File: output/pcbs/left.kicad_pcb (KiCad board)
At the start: 2 copper layers, 151.8 x 117.2 mm, 85 parts

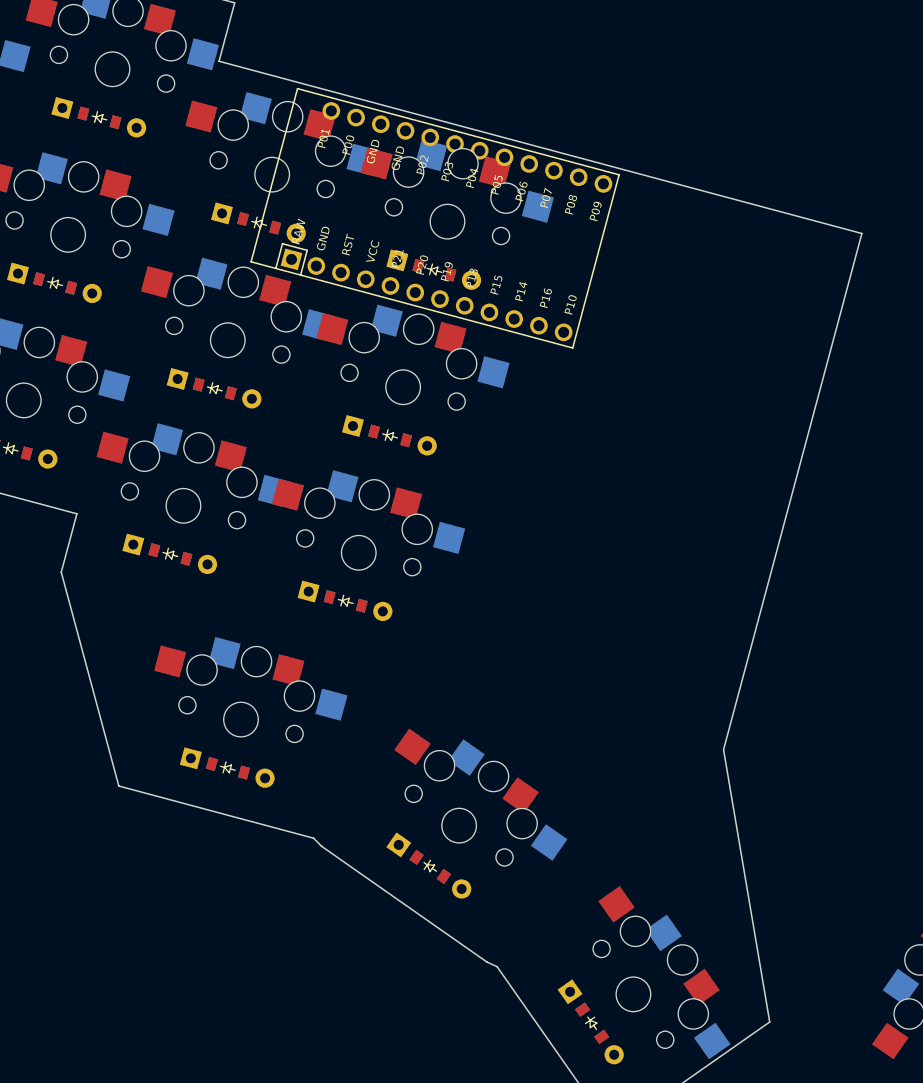
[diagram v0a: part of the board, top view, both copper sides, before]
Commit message: run ergogen with new case
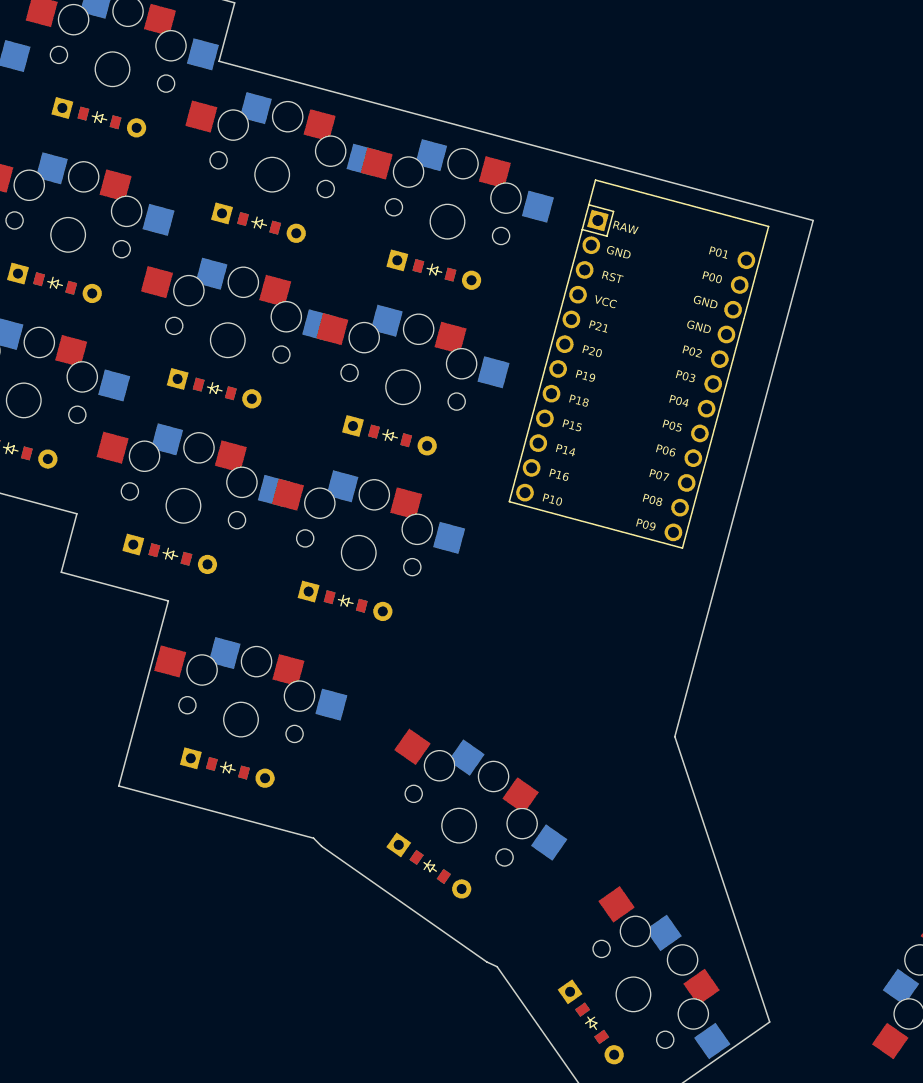
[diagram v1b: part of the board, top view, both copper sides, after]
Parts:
- moved MCU1 24.2 mm to (117.2, -4.82), turned to -105 degrees
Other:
- board size 151.8 x 117.2 mm -> 147 x 117.2 mm
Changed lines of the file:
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@@
     )
       (module ProMicro (layer F.Cu)
-      (at 98.5801815 -20.1729481 -15)
+      (at 117.2423592 -4.819670799999999 -105)
       (fp_text reference "MCU1" (at 0 0) (layer F.SilkS) hide (effects (font (size 1.27 1.27) (thickness 0.15))))
       (fp_text value "" (at 0 0) (layer F.SilkS) hide (effects (font (size 1.27 1.27) (thickness 0.15))))
@@
         (fp_line (start -15.24 6.35) (end -15.24 8.89) (layer F.SilkS) (width 0.15))
         (fp_line (start -12.7 6.35) (end -12.7 8.89) (layer F.SilkS) (width 0.15))
-        (fp_text user RAW (at -13.97 4.8 75) (layer F.SilkS) (effects (font (size 0.8 0.8) (thickness 0.15))))
-        (fp_text user GND (at -11.43 4.8 75) (layer F.SilkS) (effects (font (size 0.8 0.8) (thickness 0.15))))
-        (fp_text user RST (at -8.89 4.8 75) (layer F.SilkS) (effects (font (size 0.8 0.8) (thickness 0.15))))
-        (fp_text user VCC (at -6.35 4.8 75) (layer F.SilkS) (effects (font (size 0.8 0.8) (thickness 0.15))))
-        (fp_text user P21 (at -3.81 4.8 75) (layer F.SilkS) (effects (font (size 0.8 0.8) (thickness 0.15))))
-        (fp_text user P20 (at -1.27 4.8 75) (layer F.SilkS) (effects (font (size 0.8 0.8) (thickness 0.15))))
-        (fp_text user P19 (at 1.27 4.8 75) (layer F.SilkS) (effects (font (size 0.8 0.8) (thickness 0.15))))
-        (fp_text user P18 (at 3.81 4.8 75) (layer F.SilkS) (effects (font (size 0.8 0.8) (thickness 0.15))))
-        (fp_text user P15 (at 6.35 4.8 75) (layer F.SilkS) (effects (font (size 0.8 0.8) (thickness 0.15))))
-        (fp_text user P14 (at 8.89 4.8 75) (layer F.SilkS) (effects (font (size 0.8 0.8) (thickness 0.15))))
-        (fp_text user P16 (at 11.43 4.8 75) (layer F.SilkS) (effects (font (size 0.8 0.8) (thickness 0.15))))
-        (fp_text user P10 (at 13.97 4.8 75) (layer F.SilkS) (effects (font (size 0.8 0.8) (thickness 0.15))))
-        (fp_text user P01 (at -13.97 -4.8 75) (layer F.SilkS) (effects (font (size 0.8 0.8) (thickness 0.15))))
-        (fp_text user P00 (at -11.43 -4.8 75) (layer F.SilkS) (effects (font (size 0.8 0.8) (thickness 0.15))))
-        (fp_text user GND (at -8.89 -4.8 75) (layer F.SilkS) (effects (font (size 0.8 0.8) (thickness 0.15))))
-        (fp_text user GND (at -6.35 -4.8 75) (layer F.SilkS) (effects (font (size 0.8 0.8) (thickness 0.15))))
-        (fp_text user P02 (at -3.81 -4.8 75) (layer F.SilkS) (effects (font (size 0.8 0.8) (thickness 0.15))))
-        (fp_text user P03 (at -1.27 -4.8 75) (layer F.SilkS) (effects (font (size 0.8 0.8) (thickness 0.15))))
-        (fp_text user P04 (at 1.27 -4.8 75) (layer F.SilkS) (effects (font (size 0.8 0.8) (thickness 0.15))))
-        (fp_text user P05 (at 3.81 -4.8 75) (layer F.SilkS) (effects (font (size 0.8 0.8) (thickness 0.15))))
-        (fp_text user P06 (at 6.35 -4.8 75) (layer F.SilkS) (effects (font (size 0.8 0.8) (thickness 0.15))))
-        (fp_text user P07 (at 8.89 -4.8 75) (layer F.SilkS) (effects (font (size 0.8 0.8) (thickness 0.15))))
-        (fp_text user P08 (at 11.43 -4.8 75) (layer F.SilkS) (effects (font (size 0.8 0.8) (thickness 0.15))))
-        (fp_text user P09 (at 13.97 -4.8 75) (layer F.SilkS) (effects (font (size 0.8 0.8) (thickness 0.15))))
-        (pad 1 thru_hole rect (at -13.97 7.62 -15) (size 1.7526 1.7526) (drill 1.0922) (layers *.Cu *.SilkS *.Mask) (net 43 "RAW"))
+        (fp_text user RAW (at -13.97 4.8 -15) (layer F.SilkS) (effects (font (size 0.8 0.8) (thickness 0.15))))
+        (fp_text user GND (at -11.43 4.8 -15) (layer F.SilkS) (effects (font (size 0.8 0.8) (thickness 0.15))))
+        (fp_text user RST (at -8.89 4.8 -15) (layer F.SilkS) (effects (font (size 0.8 0.8) (thickness 0.15))))
+        (fp_text user VCC (at -6.35 4.8 -15) (layer F.SilkS) (effects (font (size 0.8 0.8) (thickness 0.15))))
+        (fp_text user P21 (at -3.81 4.8 -15) (layer F.SilkS) (effects (font (size 0.8 0.8) (thickness 0.15))))
+        (fp_text user P20 (at -1.27 4.8 -15) (layer F.SilkS) (effects (font (size 0.8 0.8) (thickness 0.15))))
+        (fp_text user P19 (at 1.27 4.8 -15) (layer F.SilkS) (effects (font (size 0.8 0.8) (thickness 0.15))))
+        (fp_text user P18 (at 3.81 4.8 -15) (layer F.SilkS) (effects (font (size 0.8 0.8) (thickness 0.15))))
+        (fp_text user P15 (at 6.35 4.8 -15) (layer F.SilkS) (effects (font (size 0.8 0.8) (thickness 0.15))))
+        (fp_text user P14 (at 8.89 4.8 -15) (layer F.SilkS) (effects (font (size 0.8 0.8) (thickness 0.15))))
+        (fp_text user P16 (at 11.43 4.8 -15) (layer F.SilkS) (effects (font (size 0.8 0.8) (thickness 0.15))))
+        (fp_text user P10 (at 13.97 4.8 -15) (layer F.SilkS) (effects (font (size 0.8 0.8) (thickness 0.15))))
+        (fp_text user P01 (at -13.97 -4.8 -15) (layer F.SilkS) (effects (font (size 0.8 0.8) (thickness 0.15))))
+        (fp_text user P00 (at -11.43 -4.8 -15) (layer F.SilkS) (effects (font (size 0.8 0.8) (thickness 0.15))))
+        (fp_text user GND (at -8.89 -4.8 -15) (layer F.SilkS) (effects (font (size 0.8 0.8) (thickness 0.15))))
+        (fp_text user GND (at -6.35 -4.8 -15) (layer F.SilkS) (effects (font (size 0.8 0.8) (thickness 0.15))))
+        (fp_text user P02 (at -3.81 -4.8 -15) (layer F.SilkS) (effects (font (size 0.8 0.8) (thickness 0.15))))
+        (fp_text user P03 (at -1.27 -4.8 -15) (layer F.SilkS) (effects (font (size 0.8 0.8) (thickness 0.15))))
+        (fp_text user P04 (at 1.27 -4.8 -15) (layer F.SilkS) (effects (font (size 0.8 0.8) (thickness 0.15))))
+        (fp_text user P05 (at 3.81 -4.8 -15) (layer F.SilkS) (effects (font (size 0.8 0.8) (thickness 0.15))))
+        (fp_text user P06 (at 6.35 -4.8 -15) (layer F.SilkS) (effects (font (size 0.8 0.8) (thickness 0.15))))
+        (fp_text user P07 (at 8.89 -4.8 -15) (layer F.SilkS) (effects (font (size 0.8 0.8) (thickness 0.15))))
+        (fp_text user P08 (at 11.43 -4.8 -15) (layer F.SilkS) (effects (font (size 0.8 0.8) (thickness 0.15))))
+        (fp_text user P09 (at 13.97 -4.8 -15) (layer F.SilkS) (effects (font (size 0.8 0.8) (thickness 0.15))))
+        (pad 1 thru_hole rect (at -13.97 7.62 -105) (size 1.7526 1.7526) (drill 1.0922) (layers *.Cu *.SilkS *.Mask) (net 43 "RAW"))
         (pad 2 thru_hole circle (at -11.43 7.62 0) (size 1.7526 1.7526) (drill 1.0922) (layers *.Cu *.SilkS *.Mask) (net 44 "GND"))
         (pad 3 thru_hole circle (at -8.89 7.62 0) (size 1.7526 1.7526) (drill 1.0922) (layers *.Cu *.SilkS *.Mask) (net 45 "RST"))
@@
 (gr_line (start 46.3737309 4.6612324) (end 61.8285441 8.802337099999999) (angle 90) (layer Edge.Cuts) (width 0.15))
 (gr_line (start 61.8285441 8.802337099999999) (end 60.275629800000004 14.597892000000002) (angle 90) (layer Edge.Cuts) (width 0.15))
-(gr_line (start 60.275629800000004 14.597892000000002) (end 65.98325200000001 35.7974923) (angle 90) (layer Edge.Cuts) (width 0.15))
+(gr_line (start 60.275629800000004 14.597892000000002) (end 70.9008139 17.4449015) (angle 90) (layer Edge.Cuts) (width 0.15))
+(gr_line (start 70.9008139 17.4449015) (end 65.98325200000001 35.7974923) (angle 90) (layer Edge.Cuts) (width 0.15))
 (gr_line (start 65.98325200000001 35.7974923) (end 85.30176850000001 40.9738732) (angle 90) (layer Edge.Cuts) (width 0.15))
 (gr_line (start 85.30176850000001 40.9738732) (end 86.09494289999999 41.7748356) (angle 90) (layer Edge.Cuts) (width 0.15))
@@
 (gr_line (start 103.50192390000001 53.717759300000004) (end 114.9734526 70.10080020000001) (angle 90) (layer Edge.Cuts) (width 0.15))
 (gr_line (start 114.9734526 70.10080020000001) (end 130.5373415 59.2028479) (angle 90) (layer Edge.Cuts) (width 0.15))
-(gr_line (start 130.5373415 59.2028479) (end 125.958586 32.1975872) (angle 90) (layer Edge.Cuts) (width 0.15))
-(gr_line (start 125.958586 32.1975872) (end 139.6759955 -18.9964816) (angle 90) (layer Edge.Cuts) (width 0.15))
-(gr_line (start 139.6759955 -18.9964816) (end 75.9248909 -36.078538699999996) (angle 90) (layer Edge.Cuts) (width 0.15))
+(gr_line (start 130.5373415 59.2028479) (end 121.1289569 30.9034919) (angle 90) (layer Edge.Cuts) (width 0.15))
+(gr_line (start 121.1289569 30.9034919) (end 134.8463663 -20.290576899999998) (angle 90) (layer Edge.Cuts) (width 0.15))
+(gr_line (start 134.8463663 -20.290576899999998) (end 75.9248909 -36.078538699999996) (angle 90) (layer Edge.Cuts) (width 0.15))
 (gr_line (start 75.9248909 -36.078538699999996) (end 77.47780519999999 -41.874093699999996) (angle 90) (layer Edge.Cuts) (width 0.15))
 (gr_line (start 77.47780519999999 -41.874093699999996) (end 58.15928869999999 -47.0504746) (angle 90) (layer Edge.Cuts) (width 0.15))

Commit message: add nrf footprint
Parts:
- MCU1: value (none) -> xiao-ble; footprint ProMicro -> XIAO-BLE
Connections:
- MCU1 pad 1: RAW -> P0
- MCU1 pad 10: P14 -> P9
- MCU1 pad 11: P16 -> P10
- MCU1 pad 12: P10 -> RAW3V3
- MCU1 pad 13: P1 -> GND
- MCU1 pad 14: P0 -> RAW5V
- MCU1 pad 15: GND -> SWCLK
- MCU1 pad 16: GND -> SWDIO
- MCU1 pad 17: P2 -> GND
- MCU1 pad 18: P3 -> RST
- MCU1 pad 19: P4 -> BAT_POS
- MCU1 pad 2: GND -> P1
- MCU1 pad 20: P5 -> BAT_NEG
- MCU1 pad 21: P6 -> NFC0
- MCU1 pad 22: P7 -> NFC1
- MCU1 pad 3: RST -> P2
- MCU1 pad 4: VCC -> P3
- MCU1 pad 5: P21 -> P4
- MCU1 pad 6: P20 -> P5
- MCU1 pad 7: P19 -> P6
- MCU1 pad 8: P18 -> P7
- MCU1 pad 9: P15 -> P8

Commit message: use kicad to export example switchplate
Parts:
- moved MCU1 8.00 mm to (119.3, -12.5), turned to -15 degrees
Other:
- net class Default removed

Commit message: redo the outlines lololol
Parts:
- added D43: , ComboDiode, F.Cu at (256.8, 63.5)
- added D44: , ComboDiode, F.Cu at (247.1, 49.5)
- added S43: , PG1350, F.Cu at (254.0, 59.4)
- added S44: , PG1350, F.Cu at (244.2, 45.4)
- moved D22 177.8 mm to (96.5, 49.5), turned to -35 degrees
- moved S22 174.0 mm to (99.4, 45.4), turned to -35 degrees
- moved S42 110.7 mm to (259.0, 35.1), turned to 35 degrees
- moved D42 109.3 mm to (261.8, 39.2), turned to 35 degrees
- moved D41 101.6 mm to (271.6, 53.1)
- moved S41 101.6 mm to (268.7, 49.0)
- moved D34 93.9 mm to (279.5, -30.5)
- moved S34 93.9 mm to (278.2, -35.3)
- moved S25 92.8 mm to (334.8, -32.8)
- moved S37 92.8 mm to (262.4, -24.8)
- moved D25 92.8 mm to (336.1, -28.0)
- moved D37 92.8 mm to (263.7, -20.0)
- moved D31 92.1 mm to (298.2, -30.3)
- moved S31 92.1 mm to (296.9, -35.1)
- moved D28 91.7 mm to (318.7, -23.4)
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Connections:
- net far_thumb renamed right_bottom
- net home_thumb renamed left_top
- net mirror_far_thumb renamed mirror_left_top
- net mirror_home_thumb renamed mirror_left_bottom
- net near_thumb renamed left_bottom
- D22 pad 2: mirror_outer_bottom -> right_top
- D23 pad 2: mirror_outer_home -> mirror_outer_bottom
- D24 pad 2: mirror_outer_top -> mirror_outer_home
- D25 pad 2: mirror_pinky_bottom -> mirror_outer_top
- D26 pad 2: mirror_pinky_home -> mirror_pinky_bottom
- D27 pad 2: mirror_pinky_top -> mirror_pinky_home
- D28 pad 2: mirror_ring_bottom -> mirror_pinky_top
- D29 pad 2: mirror_ring_home -> mirror_ring_bottom
- D30 pad 2: mirror_ring_top -> mirror_ring_home
- D31 pad 2: mirror_middle_bottom -> mirror_ring_top
- D32 pad 2: mirror_middle_home -> mirror_middle_bottom
- D33 pad 2: mirror_middle_top -> mirror_middle_home
- D34 pad 2: mirror_index_bottom -> mirror_middle_top
- D35 pad 2: mirror_index_home -> mirror_index_bottom
- D36 pad 2: mirror_index_top -> mirror_index_home
- D37 pad 2: mirror_inner_bottom -> mirror_index_top
- D38 pad 2: mirror_inner_home -> mirror_inner_bottom
- D39 pad 2: mirror_inner_top -> mirror_inner_home
- D40 pad 2: mirror_near_thumb -> mirror_inner_top
- S22 pad 2: mirror_outer_bottom -> right_top
- S23 pad 2: mirror_outer_home -> mirror_outer_bottom
- S24 pad 2: mirror_outer_top -> mirror_outer_home
- S25 pad 2: mirror_pinky_bottom -> mirror_outer_top
- S26 pad 2: mirror_pinky_home -> mirror_pinky_bottom
- S27 pad 2: mirror_pinky_top -> mirror_pinky_home
- S28 pad 2: mirror_ring_bottom -> mirror_pinky_top
- S29 pad 2: mirror_ring_home -> mirror_ring_bottom
- S30 pad 2: mirror_ring_top -> mirror_ring_home
- S31 pad 2: mirror_middle_bottom -> mirror_ring_top
- S32 pad 2: mirror_middle_home -> mirror_middle_bottom
- S33 pad 2: mirror_middle_top -> mirror_middle_home
- S34 pad 2: mirror_index_bottom -> mirror_middle_top
- S35 pad 2: mirror_index_home -> mirror_index_bottom
- S36 pad 2: mirror_index_top -> mirror_index_home
- S37 pad 2: mirror_inner_bottom -> mirror_index_top
- S38 pad 2: mirror_inner_home -> mirror_inner_bottom
- S39 pad 2: mirror_inner_top -> mirror_inner_home
- S40 pad 2: mirror_near_thumb -> mirror_inner_top
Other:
- board size 147 x 117.2 mm -> 127.7 x 136.5 mm
- net class Default added: clearance 0.2, trace_width 0.25, via_dia 0.8, via_drill 0.4

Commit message: add switchplate
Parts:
- removed MCU1: xiao-ble, XIAO-BLE
- moved D12 2.00 mm to (64.6, -32.4)
- moved S12 2.00 mm to (65.9, -37.2)
- moved D6 2.00 mm to (25.4, -25.3)
- moved D9 2.00 mm to (45.9, -32.2)
- moved S9 2.00 mm to (47.2, -37.0)
- moved S15 2.00 mm to (81.7, -26.8)
- moved S18 2.00 mm to (99.1, -22.1)
- moved S6 2.00 mm to (26.7, -30.1)
- moved D18 2.00 mm to (97.8, -17.3)
- moved D15 2.00 mm to (80.4, -21.9)
- moved D3 2.00 mm to (8.02, -29.9)
- moved S3 2.00 mm to (9.32, -34.8)
- moved D28 1.93 mm to (318.7, -25.3)
- moved D31 1.93 mm to (298.2, -32.2)
- moved D34 1.93 mm to (279.5, -32.4)
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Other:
- board size 127.7 x 136.5 mm -> 145 x 139.4 mm
